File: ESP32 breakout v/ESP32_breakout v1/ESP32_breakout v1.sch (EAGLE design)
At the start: 14 parts, among them U1 ESP-WROOM-32

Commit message: Write pins
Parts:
- U2: value (none) -> AP7361C-33E-13
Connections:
- net PROG renamed IO0
- new net CLK: U1.CLK
- new net CMD: U1.CMD
- new net IO12: U1.IO12
- new net IO13: U1.IO13
- new net IO14: U1.IO14
- new net IO15: U1.IO15
- new net IO16: U1.IO16
- new net IO17: U1.IO17
- new net IO18: U1.IO18
- new net IO19: U1.IO19
- new net IO2: U1.IO2
- new net IO21: U1.IO21
- new net IO22: U1.IO22
- new net IO23: U1.IO23
- new net IO25: U1.IO25
- new net IO26: U1.IO26
- new net IO27: U1.IO27
- new net IO34: U1.IO34
- new net IO35: U1.IO35
- new net IO4: U1.IO4
- new net IO5: U1.IO5
- new net SD0: U1.SDO
- new net SD1: U1.SD1
- new net SD2: U1.SD2
- new net SD3: U1.SD3
- new net S_VN: U1.SENSOR_VN
- new net S_VP: U1.SENSOR_VP
- net GND: now also U1.GND

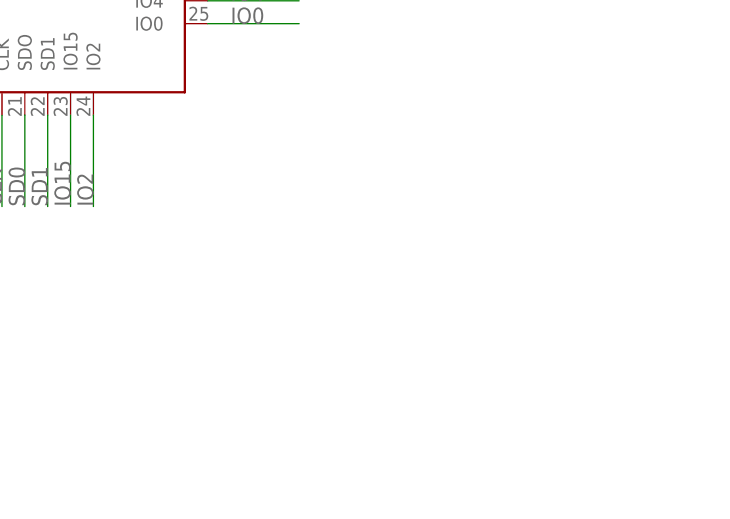
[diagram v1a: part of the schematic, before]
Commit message: Header breakouts added
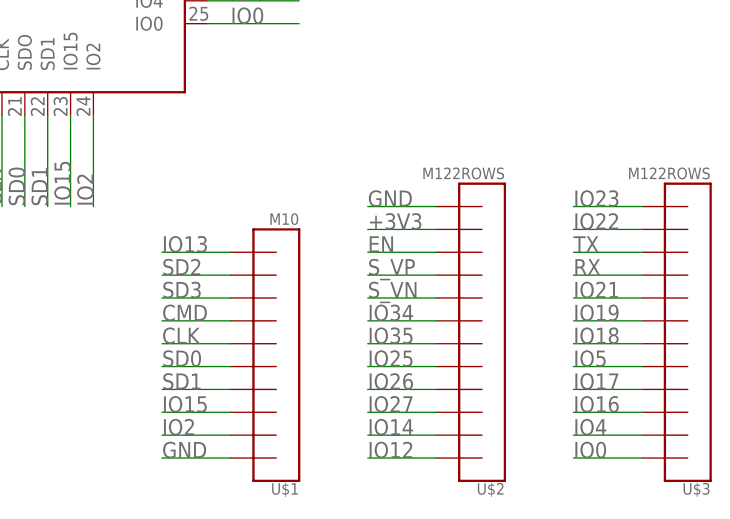
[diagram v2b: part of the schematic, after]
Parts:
- added U$1: M10, dr-library:M10
- added U$2, U$3: M122ROWS, dr-library:M122ROWS
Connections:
- net +3V3: now also U$2.11
- net CLK: now also U$1.6
- net CMD: now also U$1.7
- net EN: now also U$2.10
- net GND: now also U$1.1, U$2.12
- net IO0: now also U$3.1
- net IO12: now also U$2.1
- net IO13: now also U$1.10
- net IO14: now also U$2.2
- net IO15: now also U$1.3
- net IO16: now also U$3.3
- net IO17: now also U$3.4
- net IO18: now also U$3.6
- net IO19: now also U$3.7
- net IO2: now also U$1.2
- net IO21: now also U$3.8
- net IO22: now also U$3.11
- net IO23: now also U$3.12
- net IO25: now also U$2.5
- net IO26: now also U$2.4
- net IO27: now also U$2.3
- net IO34: now also U$2.7
- net IO35: now also U$2.6
- net IO4: now also U$3.2
- net IO5: now also U$3.5
- net RX: now also U$3.9
- net SD0: now also U$1.5
- net SD1: now also U$1.4
- net SD2: now also U$1.9
- net SD3: now also U$1.8
- net S_VN: now also U$2.8
- net S_VP: now also U$2.9
- net TX: now also U$3.10

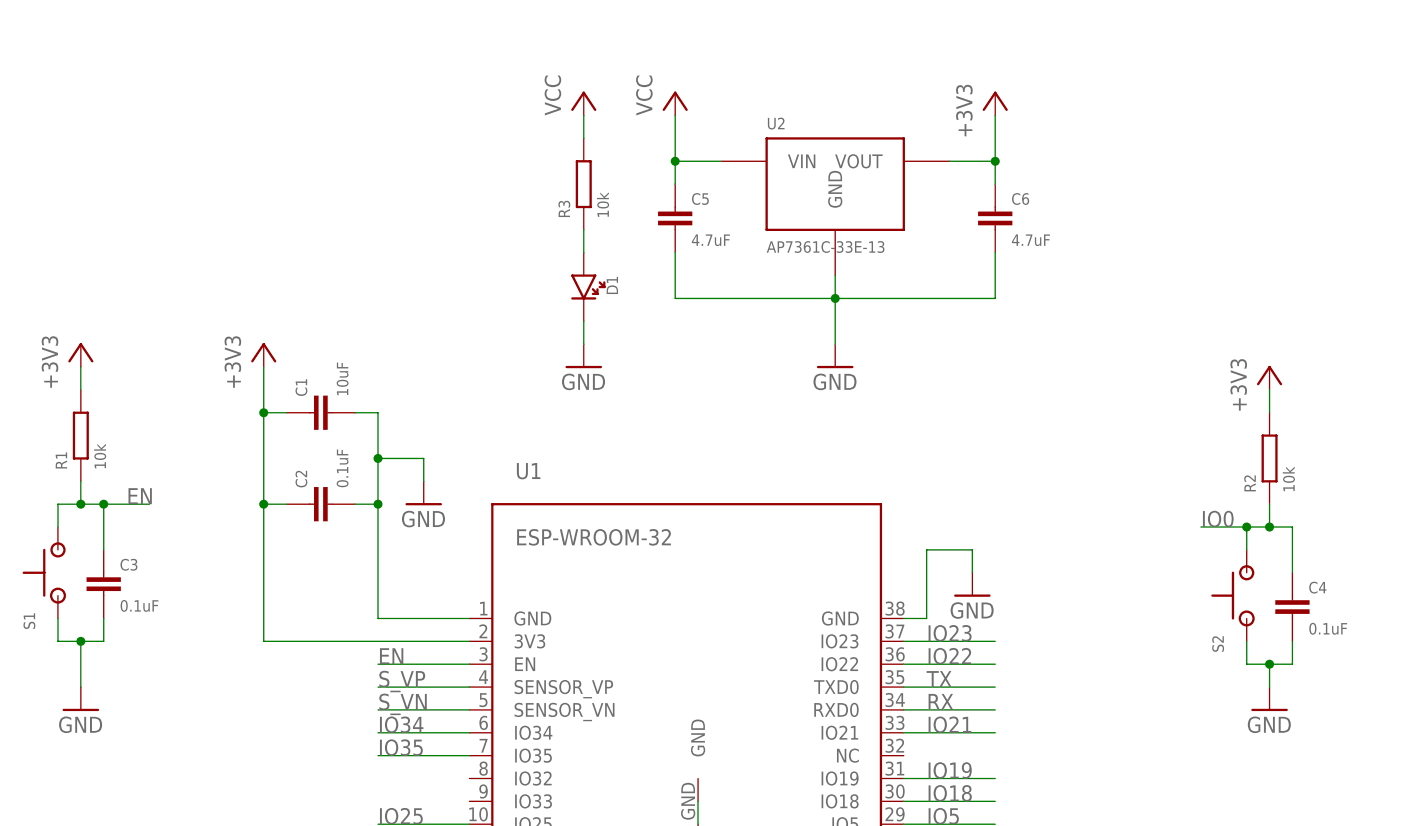
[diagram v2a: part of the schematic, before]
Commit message: Rough component placement
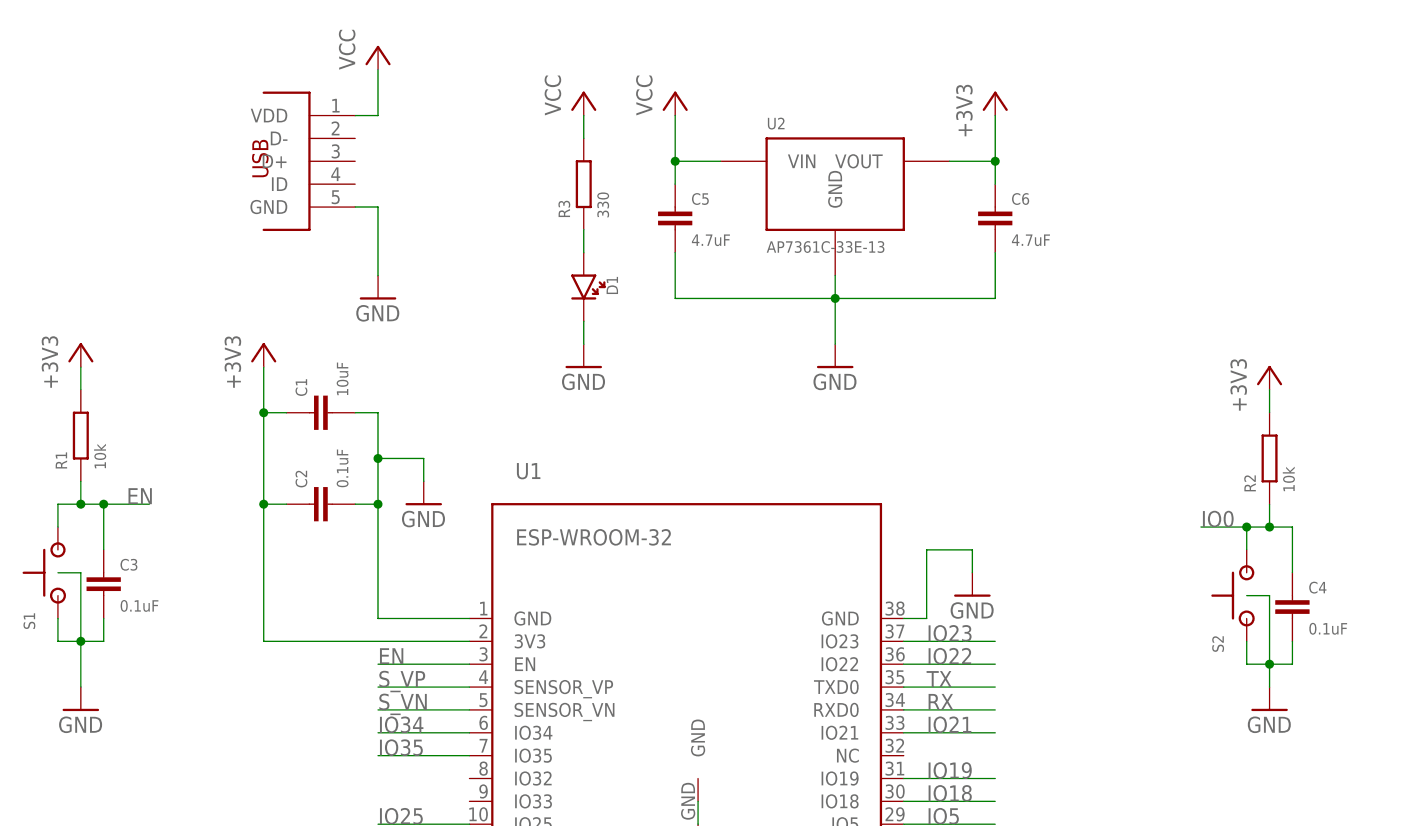
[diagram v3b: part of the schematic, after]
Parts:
- added U$4: MOLEX_USBMICRO, dr-library:MOLEX_USBMICRO
- R3: value 10k -> 330
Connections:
- net GND: now also S1.3, S2.3, U$4.GND
- net VCC: now also U$4.VDD
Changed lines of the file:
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@@
 <part name="C6" library="dr-library" deviceset="CAP" device="0603" value="4.7uF"/>
 <part name="D1" library="dr-library" deviceset="LED" device="1206"/>
-<part name="R3" library="dr-library" deviceset="RESISTOR" device="0603" value="10k"/>
+<part name="R3" library="dr-library" deviceset="RESISTOR" device="0603" value="330"/>
 <part name="+3V4" library="supply1" deviceset="+3V3" device=""/>
 <part name="GND6" library="supply1" deviceset="GND" device=""/>
@@
 <part name="U$2" library="dr-library" deviceset="M12" device="2ROWS"/>
 <part name="U$3" library="dr-library" deviceset="M12" device="2ROWS"/>
+<part name="U$4" library="dr-library" deviceset="MOLEX_USBMICRO" device=""/>
+<part name="P+3" library="supply1" deviceset="VCC" device=""/>
+<part name="GND9" library="supply1" deviceset="GND" device=""/>
 </parts>
 <sheets>
@@
 <instance part="U$2" gate="G$1" x="104.14" y="-2.54" rot="R180"/>
 <instance part="U$3" gate="G$1" x="127" y="-2.54" rot="R180"/>
+<instance part="U$4" gate="G$1" x="7.62" y="116.84" rot="R180"/>
+<instance part="P+3" gate="VCC" x="15.24" y="124.46"/>
+<instance part="GND9" gate="1" x="15.24" y="96.52"/>
 </instances>
 <busses>
@@
 <junction x="-17.78" y="58.42"/>
 <pinref part="GND3" gate="1" pin="GND"/>
+<pinref part="S1" gate="G$1" pin="3"/>
+<wire x1="-20.32" y1="66.04" x2="-17.78" y2="66.04" width="0.1524" layer="91"/>
+<wire x1="-17.78" y1="66.04" x2="-17.78" y2="58.42" width="0.1524" layer="91"/>
 </segment>
 <segment>
@@
 <wire x1="114.3" y1="55.88" x2="114.3" y2="53.34" width="0.1524" layer="91"/>
 <junction x="114.3" y="55.88"/>
+<pinref part="S2" gate="G$1" pin="3"/>
+<wire x1="111.76" y1="63.5" x2="114.3" y2="63.5" width="0.1524" layer="91"/>
+<wire x1="114.3" y1="63.5" x2="114.3" y2="55.88" width="0.1524" layer="91"/>
 </segment>
 <segment>
@@
 <wire x1="99.06" y1="7.62" x2="91.44" y2="7.62" width="0.1524" layer="91"/>
 <label x="91.44" y="7.62" size="1.778" layer="95"/>
+</segment>
+<segment>
+<pinref part="U$4" gate="G$1" pin="GND"/>
+<wire x1="12.7" y1="106.68" x2="15.24" y2="106.68" width="0.1524" layer="91"/>
+<wire x1="15.24" y1="106.68" x2="15.24" y2="99.06" width="0.1524" layer="91"/>
+<pinref part="GND9" gate="1" pin="GND"/>
 </segment>
 </net>
@@
 <pinref part="P+2" gate="VCC" pin="VCC"/>
 </segment>
-</net>
+<segment>
+<pinref part="U$4" gate="G$1" pin="VDD"/>
+<wire x1="12.7" y1="116.84" x2="15.24" y2="116.84" width="0.1524" layer="91"/>
+<wire x1="15.24" y1="116.84" x2="15.24" y2="121.92" width="0.1524" layer="91"/>
+<pinref part="P+3" gate="VCC" pin="VCC"/>
+</segment>
+</net>

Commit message: Added USB ccomponents
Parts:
- added C7, C8: 22pF, dr-library:CAP0603
- added C9: 0.1uF, dr-library:CAP0603
- added U$5, U$6: M06, dr-library:M06
- added U$7: CH340G, usb-serial:CH340G
- added Y1: (no value), dr-library:LFXTAL061647-R
- U$1: value M10 -> M09; device dr-library:M10 -> dr-library:M09
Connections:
- new net N$3: C7.1, U$7.XI, Y1.1
- new net N$4: C8.1, U$7.XO, Y1.2
- new net N$5: U$4.D+, U$7.D+
- new net N$6: U$4.D-, U$7.D-
- net +3V3: now also C9.2, U$7.V3, U$7.VCC
- net CLK: now also U$1.5; no longer U$1.6
- net CMD: now also U$1.6; no longer U$1.7
- net GND: now also C7.2, C8.2, C9.1, U$7.GND, Y1.GND@2, Y1.GND@4; no longer U$1.1
- net IO12: now also U$6.4
- net IO13: now also U$1.9, U$6.6; no longer U$1.10
- net IO14: now also U$6.5
- net IO15: now also U$1.2, U$6.1; no longer U$1.3
- net IO18: now also U$5.5
- net IO19: now also U$5.4
- net IO2: now also U$1.1, U$6.2; no longer U$1.2
- net IO21: now also U$5.3
- net IO22: now also U$5.2
- net IO23: now also U$5.6
- net IO4: now also U$6.3
- net IO5: now also U$5.1
- net RX: now also U$7.RX
- net SD0: now also U$1.4; no longer U$1.5
- net SD1: now also U$1.3; no longer U$1.4
- net SD2: now also U$1.8; no longer U$1.9
- net SD3: now also U$1.7; no longer U$1.8
- net TX: now also U$7.TX
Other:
- note added: "HSPI"
- note added: "HSPICLK"
- note added: "HSPICS"
- note added: "HSPID"
- note added: "HSPIHD"
- note added: "HSPIQ"
- note added: "HSPIWP"
- note added: "VSPI"
- note added: "VSPICLK"
- note added: "VSPICS"
- note added: "VSPID"
- note added: "VSPIHD"
- note added: "VSPIQ"
- note added: "VSPIWP"

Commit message: layout
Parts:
- added U$14, U$15: M05, dr-library:M05
- added U$8: SCHA4B0419, dr-library:SCHA4B0419
- added U$9: M02LONG, dr-library:M02LONG
- C5, C6: value 4.7uF -> 10uF; device dr-library:CAP0603 -> dr-library:CAP-POLARCASEB-3528
- U$1: value M09 -> M02LONG; device dr-library:M09 -> dr-library:M02LONG
- U2: value AP7361C-33E-13 -> (none); device dr-library:AP7361C-33E-13 -> dr-library:REG-1117
- Y1: value (none) -> 12MHz; device dr-library:LFXTAL061647-R -> dr-library:ABLS-12MHZ-B2-T
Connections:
- net +3V3: now also C6.P, U$8.VDD, U$9.2, U2.TAB; no longer C6.1
- net CLK: now also U$14.1, U$8.CLK; no longer U$1.5
- net CMD: now also U$15.5, U$8.CMD; no longer U$1.6
- net GND: now also C5.N, C6.N, U$1.1, U$15.1, U$8.GND, U$8.GND1, U$8.GND2, U$9.1; no longer C5.2, C6.2, Y1.GND@2, Y1.GND@4
- net IO0: now also U$3.2; no longer U$3.1
- net IO13: now also U$15.2; no longer U$1.9
- net IO15: now also U$14.4; no longer U$1.2
- net IO16: now also U$3.4; no longer U$3.3
- net IO17: now also U$3.3; no longer U$3.4
- net IO18: now also U$3.5; no longer U$3.6
- net IO19: now also U$3.8; no longer U$3.7
- net IO2: now also U$14.5; no longer U$1.1
- net IO21: now also U$3.7; no longer U$3.8
- net IO22: now also U$3.12; no longer U$3.11
- net IO23: now also U$3.11; no longer U$3.12
- net IO4: now also U$3.1; no longer U$3.2
- net IO5: now also U$3.6; no longer U$3.5
- net RX: now also U$3.10; no longer U$3.9
- net SD0: now also U$14.2, U$8.DAT0; no longer U$1.4
- net SD1: now also U$14.3, U$8.DAT1; no longer U$1.3
- net SD2: now also U$15.3, U$8.DAT2; no longer U$1.8
- net SD3: now also U$15.4, U$8.DAT3/CMD; no longer U$1.7
- net TX: now also U$3.9; no longer U$3.10
- net VCC: now also C5.P, U$1.2; no longer C5.1

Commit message: Finish layout
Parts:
- U2: device dr-library:REG-1117 -> dr-library:NCP-1117
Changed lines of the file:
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@@
 <part name="U$8" library="dr-library" deviceset="SCHA4B0419" device=""/>
 <part name="GND12" library="supply1" deviceset="GND" device=""/>
-<part name="U2" library="dr-library" deviceset="REG-1117" device=""/>
+<part name="U2" library="dr-library" deviceset="NCP-1117" device=""/>
 <part name="C5" library="dr-library" deviceset="CAP-POLAR" device="CASEB-3528" value="10uF"/>
 <part name="C6" library="dr-library" deviceset="CAP-POLAR" device="CASEB-3528" value="10uF"/>
